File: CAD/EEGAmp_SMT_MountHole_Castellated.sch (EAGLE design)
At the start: 16 parts, among them U1 TL084QD

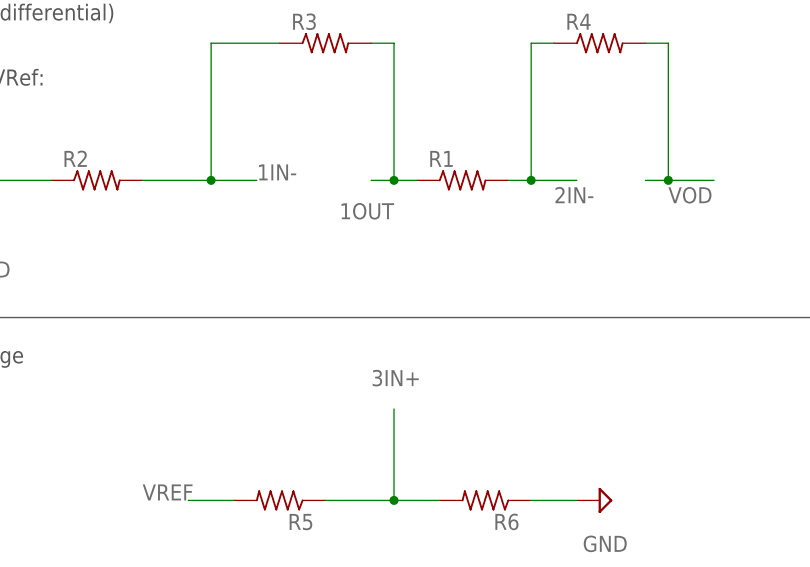
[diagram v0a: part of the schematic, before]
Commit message: added a filter cap on inputs
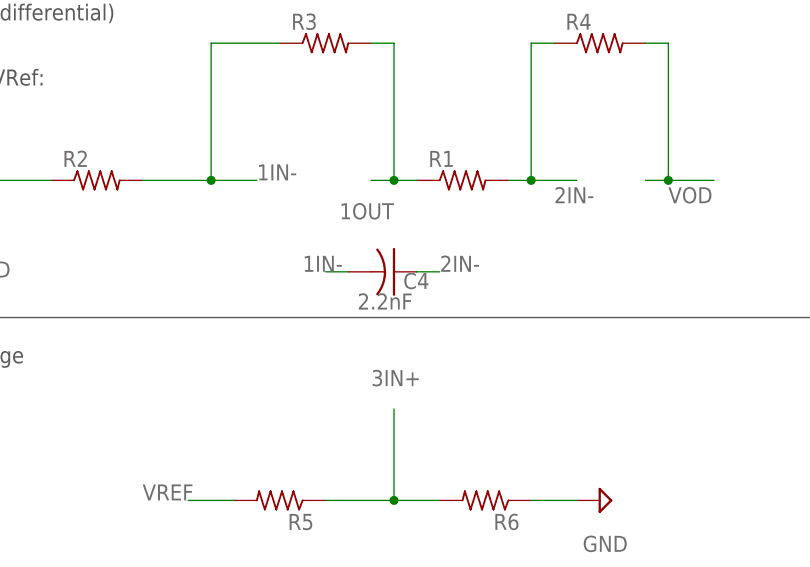
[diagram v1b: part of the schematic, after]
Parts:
- added C4: 2.2nF, rcl:C-USC0402
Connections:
- net 1IN-: now also C4.2
- net 2IN-: now also C4.1
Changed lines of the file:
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@@
 <part name="H1" library="holes" deviceset="MOUNT-PAD-ROUND" device="4.1"/>
 <part name="REFOUT" library="testpad" library_urn="urn:adsk.eagle:library:385" deviceset="PTR1" device="PAD1-17" package3d_urn="urn:adsk.eagle:package:27949/1" value="PTR1PAD1-17"/>
+<part name="C4" library="rcl" library_urn="urn:adsk.eagle:library:334" deviceset="C-US" device="C0402" package3d_urn="urn:adsk.eagle:package:23626/2" value="2.2nF"/>
 </parts>
 <sheets>
@@
 <attribute name="TP_SIGNAL_NAME" x="142.24" y="11.43" size="1.778" layer="97" rot="R270"/>
 </instance>
+<instance part="C4" gate="G$1" x="81.28" y="83.82" smashed="yes" rot="R270">
+<attribute name="NAME" x="82.296" y="81.915" size="1.778" layer="95"/>
+<attribute name="VALUE" x="77.216" y="79.629" size="1.778" layer="96"/>
+</instance>
 </instances>
 <busses>
@@
 <junction x="96.52" y="93.98"/>
 <label x="99.06" y="91.44" size="1.778" layer="95"/>
+</segment>
+<segment>
+<pinref part="C4" gate="G$1" pin="1"/>
+<wire x1="83.82" y1="83.82" x2="86.36" y2="83.82" width="0.1524" layer="91"/>
+<label x="86.36" y="83.82" size="1.778" layer="95"/>
 </segment>
 </net>
@@
 <junction x="60.96" y="93.98"/>
 </segment>
-</net>
+<segment>
+<pinref part="C4" gate="G$1" pin="2"/>
+<wire x1="76.2" y1="83.82" x2="73.66" y2="83.82" width="0.1524" layer="91"/>
+<label x="71.12" y="83.82" size="1.778" layer="95"/>
+</segment>
+</net>
